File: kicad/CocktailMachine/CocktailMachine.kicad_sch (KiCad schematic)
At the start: 39 parts, among them J1 Conn_01x08_Male, J2 0022232041, J3 3220-10-0100-00, J7 0022232041, U1 ESP32-WROOM-32, U2 TXB0104PWR, U3 MCP6477, U4 TXB0104PWR

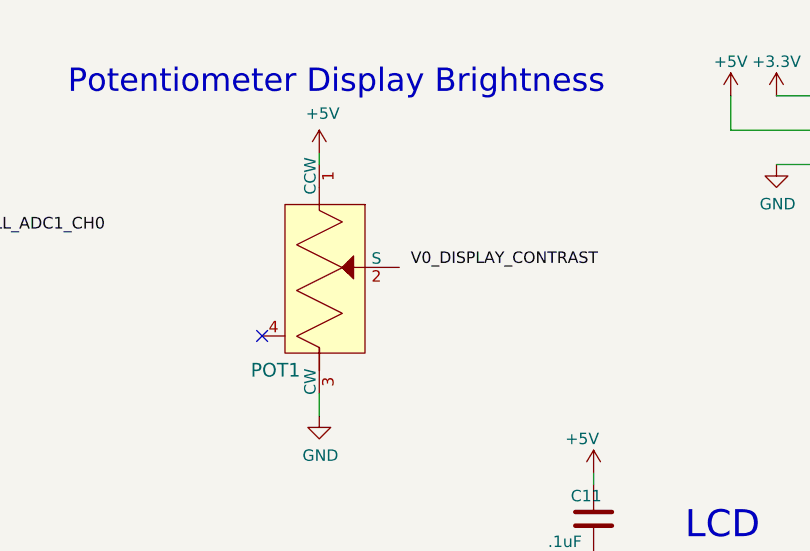
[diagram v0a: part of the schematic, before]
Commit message: - Fix DRC violations - Shrink space between modules to reduce board size
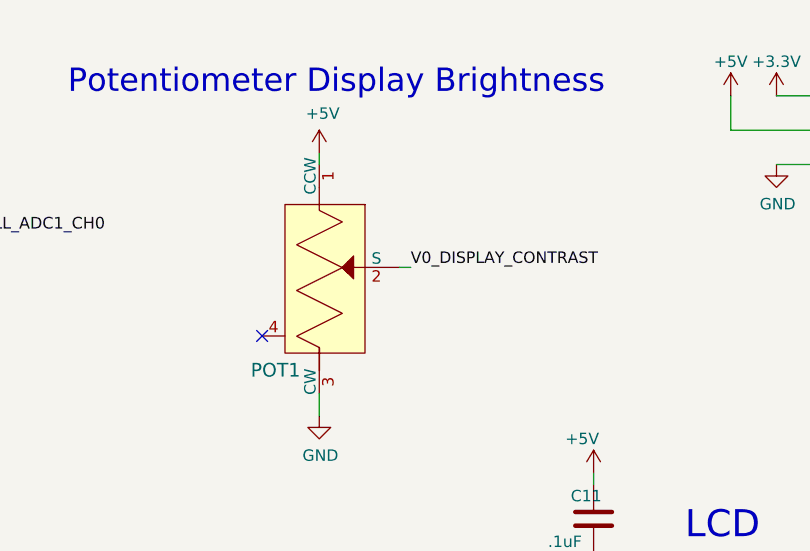
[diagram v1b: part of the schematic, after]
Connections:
- net V0_DISPLAY_CONTRAST: now also POT1.2 (S)
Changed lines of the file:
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@@
+    (stroke (width 0) (type default) (color 0 0 0 0))
+  )
+  (wire (pts (xy 222.25 41.91) (xy 223.52 41.91))
     (stroke (width 0) (type default) (color 0 0 0 0))
   )
